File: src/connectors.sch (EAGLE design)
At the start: 11 parts, among them CON1 CON-4P-TABS-JST_GH-RA, CON11 PINHEAD_1X03-2, CON12 PINHEAD_1X03-2, CON3 CON-4P-TABS-JST_GH-RA, IC6 TJA1051-HVSON8, IC8 TPD3S014DBVR-SOT23-6

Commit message: connectors PCB routing effort
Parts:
- removed CON11, CON12: PINHEAD_1X03-2, pinhead:PINHEAD_1X03-2
- added CON2: CON-4P-TABS-JST_GH-RA, Connectors:CON-4P-TABS-JST_GH-RA
- added CON4: PINHEAD_1X04-2, pinhead:PINHEAD_1X04-2
- CON3: value CON-4P-TABS-JST_GH-RA -> PINHEAD_1X04-2; device Connectors:CON-4P-TABS-JST_GH-RA -> pinhead:PINHEAD_1X04-2
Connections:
- net CAN1_RX: now also CON3.3
- net CAN1_TX: now also CON3.4
- net CAN1_VDD: now also CON2.1; no longer CON3.1
- net GND: now also CON2.4, CON2.GND, CON3.2; no longer CON3.4, CON3.GND
- net N$23: now also CON2.2; no longer CON3.2
- net N$25: now also CON2.3; no longer CON3.3
- net VDD_5V: now also CON3.1
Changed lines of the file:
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@@
 <part name="IC6" library="serial_interfaces" library_urn="urn:adsk.eagle:library:4770999" deviceset="TJA1051" device="-HVSON8" package3d_urn="urn:adsk.eagle:package:1040194/3"/>
 <part name="CON1" library="Connectors" library_urn="urn:adsk.eagle:library:3750510" deviceset="CON-4P-TABS" device="-RA" package3d_urn="urn:adsk.eagle:package:1040150/6" technology="-JST_GH"/>
-<part name="CON3" library="Connectors" library_urn="urn:adsk.eagle:library:3750510" deviceset="CON-4P-TABS" device="-RA" package3d_urn="urn:adsk.eagle:package:1040150/6" technology="-JST_GH"/>
+<part name="CON2" library="Connectors" library_urn="urn:adsk.eagle:library:3750510" deviceset="CON-4P-TABS" device="-RA" package3d_urn="urn:adsk.eagle:package:1040150/6" technology="-JST_GH"/>
 <part name="+P9" library="supply_symbols" library_urn="urn:adsk.eagle:library:13097679" deviceset="5V" device=""/>
 <part name="IC8" library="misc" library_urn="urn:adsk.eagle:library:5347860" deviceset="TPD3S014DBVR" device="-SOT23-6" package3d_urn="urn:adsk.eagle:package:1040217/3"/>
@@
 </part>
 <part name="FRAME3" library="frames" library_urn="urn:adsk.eagle:library:229" deviceset="A4L-LOC" device=""/>
-<part name="CON11" library="pinhead" library_urn="urn:adsk.eagle:library:2540341" deviceset="PINHEAD_1X03" device="-2" package3d_urn="urn:adsk.eagle:package:4854341/3"/>
-<part name="CON12" library="pinhead" library_urn="urn:adsk.eagle:library:2540341" deviceset="PINHEAD_1X03" device="-2" package3d_urn="urn:adsk.eagle:package:4854341/3"/>
+<part name="CON3" library="pinhead" library_urn="urn:adsk.eagle:library:2540341" deviceset="PINHEAD_1X04" device="-2" package3d_urn="urn:adsk.eagle:package:4854340/4"/>
+<part name="CON4" library="pinhead" library_urn="urn:adsk.eagle:library:2540341" deviceset="PINHEAD_1X04" device="-2" package3d_urn="urn:adsk.eagle:package:4854340/4"/>
 <part name="GND1" library="supply_symbols" library_urn="urn:adsk.eagle:library:13097679" deviceset="GND" device="" value="GND"/>
 <part name="GND2" library="supply_symbols" library_urn="urn:adsk.eagle:library:13097679" deviceset="GND" device="" value="GND"/>
@@
 <part name="GND5" library="supply_symbols" library_urn="urn:adsk.eagle:library:13097679" deviceset="GND" device="" value="GND"/>
 <part name="GND6" library="supply_symbols" library_urn="urn:adsk.eagle:library:13097679" deviceset="GND" device="" value="GND"/>
+<part name="+P1" library="supply_symbols" library_urn="urn:adsk.eagle:library:13097679" deviceset="5V" device=""/>
+<part name="GND7" library="supply_symbols" library_urn="urn:adsk.eagle:library:13097679" deviceset="GND" device="" value="GND"/>
 </parts>
 <sheets>
@@
 <attribute name="NAME" x="163.83" y="90.17" size="1.778" layer="95" font="vector" ratio="15" rot="R90" align="center"/>
 </instance>
-<instance part="CON3" gate="G$1" x="157.48" y="71.12" smashed="yes" rot="R270">
+<instance part="CON2" gate="G$1" x="157.48" y="71.12" smashed="yes" rot="R270">
 <attribute name="NAME" x="163.83" y="64.77" size="1.778" layer="95" font="vector" ratio="15" rot="R90" align="center"/>
 </instance>
@@
 <attribute name="SHEET" x="230.505" y="5.08" size="2.54" layer="94"/>
 </instance>
-<instance part="CON11" gate="G$1" x="50.8" y="121.92" smashed="yes">
-<attribute name="NAME" x="53.34" y="133.35" size="1.778" layer="95" font="vector" ratio="15" align="center"/>
-</instance>
-<instance part="CON12" gate="G$1" x="50.8" y="106.68" smashed="yes">
-<attribute name="NAME" x="53.34" y="118.11" size="1.778" layer="95" font="vector" ratio="15" align="center"/>
+<instance part="CON3" gate="G$1" x="50.8" y="142.24" smashed="yes" rot="MR180">
+<attribute name="NAME" x="53.34" y="128.27" size="1.778" layer="95" font="vector" ratio="15" rot="MR180" align="center"/>
+</instance>
+<instance part="CON4" gate="G$1" x="50.8" y="121.92" smashed="yes" rot="MR180">
+<attribute name="NAME" x="53.34" y="107.95" size="1.778" layer="95" font="vector" ratio="15" rot="MR180" align="center"/>
 </instance>
 <instance part="GND1" gate="1" x="144.78" y="53.34" smashed="yes">
@@
 <instance part="GND6" gate="1" x="144.78" y="109.22" smashed="yes">
 <attribute name="VALUE" x="144.78" y="107.188" size="1.016" layer="96" font="vector" ratio="15" align="center"/>
+</instance>
+<instance part="+P1" gate="G$1" x="60.96" y="142.24" smashed="yes">
+<attribute name="VALUE" x="60.96" y="145.796" size="1.27" layer="96" font="vector" ratio="15" align="center"/>
+</instance>
+<instance part="GND7" gate="1" x="60.96" y="137.16" smashed="yes" rot="MR270">
+<attribute name="VALUE" x="62.992" y="137.16" size="1.016" layer="96" font="vector" ratio="15" rot="MR270" align="center"/>
 </instance>
 </instances>
@@
 <wire x1="144.78" y1="60.96" x2="144.78" y2="86.36" width="0.1524" layer="91"/>
 <pinref part="CON1" gate="G$1" pin="4"/>
-<pinref part="CON3" gate="G$1" pin="4"/>
+<pinref part="CON2" gate="G$1" pin="4"/>
 <pinref part="GND1" gate="1" pin="GND"/>
 </segment>
 <segment>
 <wire x1="160.02" y1="53.34" x2="160.02" y2="55.88" width="0.1524" layer="91"/>
-<pinref part="CON3" gate="G$1" pin="GND"/>
+<pinref part="CON2" gate="G$1" pin="GND"/>
 <pinref part="GND2" gate="1" pin="GND"/>
 </segment>
@@
 <pinref part="GND6" gate="1" pin="GND"/>
 </segment>
+<segment>
+<pinref part="CON3" gate="G$1" pin="2"/>
+<wire x1="58.42" y1="137.16" x2="60.96" y2="137.16" width="0.1524" layer="91"/>
+<pinref part="GND7" gate="1" pin="GND"/>
+</segment>
 </net>
 <net name="CAN1_TX" class="0">
@@
 <pinref part="IC6" gate="G$1" pin="TXD"/>
 </segment>
+<segment>
+<pinref part="CON3" gate="G$1" pin="4"/>
+<wire x1="58.42" y1="132.08" x2="63.5" y2="132.08" width="0.1524" layer="91"/>
+<label x="63.5" y="132.08" size="1.27" layer="95" xref="yes"/>
+</segment>
 </net>
 <net name="CAN1_RX" class="0">
@@
 <label x="109.22" y="86.36" size="1.27" layer="95" rot="R180" xref="yes"/>
 <pinref part="IC6" gate="G$1" pin="RXD"/>
+</segment>
+<segment>
+<pinref part="CON3" gate="G$1" pin="3"/>
+<wire x1="58.42" y1="134.62" x2="63.5" y2="134.62" width="0.1524" layer="91"/>
+<label x="63.5" y="134.62" size="1.27" layer="95" xref="yes"/>
 </segment>
 </net>
@@
 <pinref part="IC6" gate="G$1" pin="CANH"/>
 <pinref part="CON1" gate="G$1" pin="2"/>
-<pinref part="CON3" gate="G$1" pin="2"/>
+<pinref part="CON2" gate="G$1" pin="2"/>
 </segment>
 </net>
@@
 <pinref part="IC6" gate="G$1" pin="CANL"/>
 <pinref part="CON1" gate="G$1" pin="3"/>
-<pinref part="CON3" gate="G$1" pin="3"/>
+<pinref part="CON2" gate="G$1" pin="3"/>
 </segment>
 </net>
@@
 <wire x1="104.14" y1="116.84" x2="104.14" y2="119.38" width="0.1524" layer="91"/>
 <junction x="104.14" y="119.38"/>
+</segment>
+<segment>
+<pinref part="CON3" gate="G$1" pin="1"/>
+<wire x1="58.42" y1="139.7" x2="60.96" y2="139.7" width="0.1524" layer="91"/>
+<pinref part="+P1" gate="G$1" pin="VDD_5V"/>
+<wire x1="60.96" y1="139.7" x2="60.96" y2="142.24" width="0.1524" layer="91"/>
 </segment>
 </net>
@@
 <wire x1="152.4" y1="68.58" x2="154.94" y2="68.58" width="0.1524" layer="91"/>
 <pinref part="CON1" gate="G$1" pin="1"/>
-<pinref part="CON3" gate="G$1" pin="1"/>
+<pinref part="CON2" gate="G$1" pin="1"/>
 <wire x1="152.4" y1="93.98" x2="152.4" y2="119.38" width="0.1524" layer="91"/>
 <junction x="152.4" y="93.98"/>

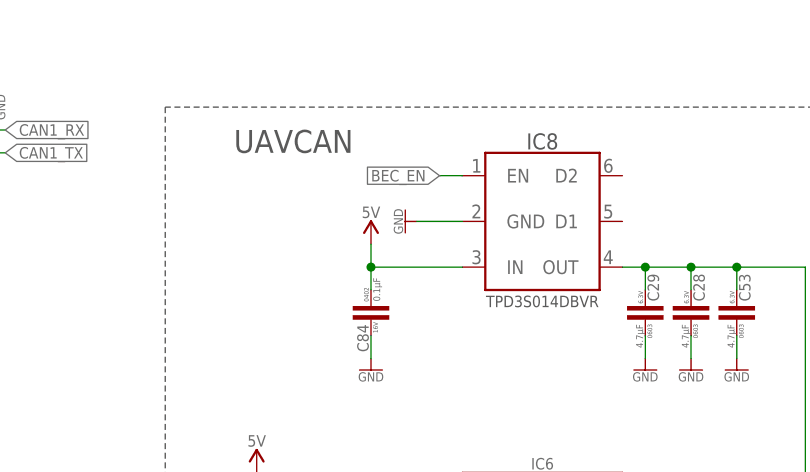
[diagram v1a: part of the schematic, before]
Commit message: connectors pcb adjustments
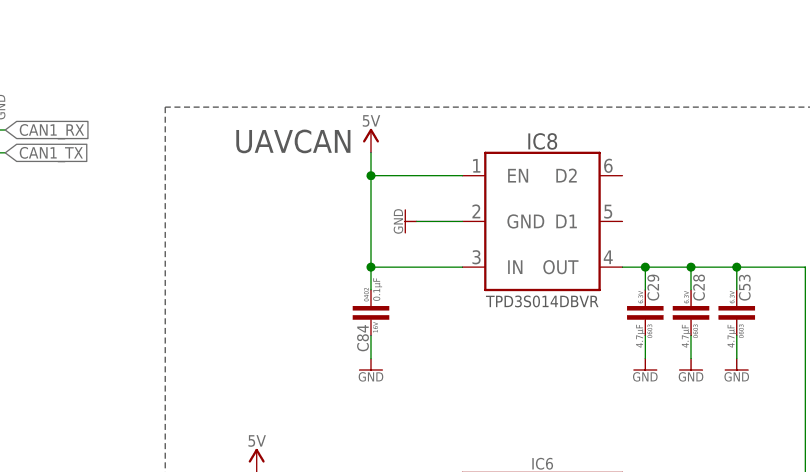
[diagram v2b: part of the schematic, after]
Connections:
- removed net BEC_EN: IC8.EN
- net VDD_5V: now also IC8.EN
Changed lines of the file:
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@@
 <attribute name="VALUE" x="107.188" y="124.46" size="1.016" layer="96" font="vector" ratio="15" rot="MR90" align="center"/>
 </instance>
-<instance part="+P10" gate="G$1" x="104.14" y="121.92" smashed="yes" rot="MR0">
-<attribute name="VALUE" x="104.14" y="125.476" size="1.27" layer="96" font="vector" ratio="15" rot="MR0" align="center"/>
+<instance part="+P10" gate="G$1" x="104.14" y="132.08" smashed="yes" rot="MR0">
+<attribute name="VALUE" x="104.14" y="135.636" size="1.27" layer="96" font="vector" ratio="15" rot="MR0" align="center"/>
 </instance>
 <instance part="C84" gate="G$1" x="104.14" y="114.3" smashed="yes" rot="R270">
@@
 <wire x1="114.3" y1="119.38" x2="104.14" y2="119.38" width="0.1524" layer="91"/>
 <pinref part="+P10" gate="G$1" pin="VDD_5V"/>
-<wire x1="104.14" y1="121.92" x2="104.14" y2="119.38" width="0.1524" layer="91"/>
+<wire x1="104.14" y1="132.08" x2="104.14" y2="129.54" width="0.1524" layer="91"/>
 <pinref part="C84" gate="G$1" pin="1"/>
+<wire x1="104.14" y1="129.54" x2="104.14" y2="119.38" width="0.1524" layer="91"/>
 <wire x1="104.14" y1="116.84" x2="104.14" y2="119.38" width="0.1524" layer="91"/>
 <junction x="104.14" y="119.38"/>
+<pinref part="IC8" gate="G$1" pin="EN"/>
+<wire x1="114.3" y1="129.54" x2="104.14" y2="129.54" width="0.1524" layer="91"/>
+<junction x="104.14" y="129.54"/>
 </segment>
 <segment>
@@
 </segment>
 </net>
-<net name="BEC_EN" class="0">
-<segment>
-<pinref part="IC8" gate="G$1" pin="EN"/>
-<wire x1="114.3" y1="129.54" x2="111.76" y2="129.54" width="0.1524" layer="91"/>
-<label x="111.76" y="129.54" size="1.27" layer="95" rot="R180" xref="yes"/>
-</segment>
-</net>

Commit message: Outline updates to allow debug assembly with connectors
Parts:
- CON3, CON4: value PINHEAD_1X04-2 -> PINHEAD_1X04-2-FEMALE; device pinhead:PINHEAD_1X04-2 -> pinhead:PINHEAD_1X04-2-FEMALE
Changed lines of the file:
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@@
 </attributes>
 <variantdefs>
-<variantdef name="basic" current="yes"/>
+<variantdef name="basic"/>
 </variantdefs>
 <classes>
@@
 </part>
 <part name="FRAME3" library="frames" library_urn="urn:adsk.eagle:library:229" deviceset="A4L-LOC" device=""/>
-<part name="CON3" library="pinhead" library_urn="urn:adsk.eagle:library:2540341" deviceset="PINHEAD_1X04" device="-2" package3d_urn="urn:adsk.eagle:package:4854340/4">
+<part name="CON3" library="pinhead" library_urn="urn:adsk.eagle:library:2540341" deviceset="PINHEAD_1X04" device="-2-FEMALE" package3d_urn="urn:adsk.eagle:package:6503396/2" value="PINHEAD_1X04-2-FEMALE">
 <variant name="basic" populate="no"/>
 </part>
-<part name="CON4" library="pinhead" library_urn="urn:adsk.eagle:library:2540341" deviceset="PINHEAD_1X04" device="-2" package3d_urn="urn:adsk.eagle:package:4854340/4">
+<part name="CON4" library="pinhead" library_urn="urn:adsk.eagle:library:2540341" deviceset="PINHEAD_1X04" device="-2-FEMALE" package3d_urn="urn:adsk.eagle:package:6503396/2" value="PINHEAD_1X04-2-FEMALE">
 <variant name="basic" populate="no"/>
 </part>
